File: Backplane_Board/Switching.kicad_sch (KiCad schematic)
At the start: 20 parts, among them J30 Conn_01x02, J31 Conn_01x02, Q3 ZXMN3A14F, Q4 ZXMN3A14F

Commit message: ready for final schmatic review
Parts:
- added C22, C23, C24, C25: 2.2uF+/35V+, Capacitor_SMD:C_0805_2012Metric, symbol Adafruit MOSFET Driver STEMMA Breakout-eagle-import:CAP_CERAMIC0805-NOOUTLINE
- added D16, D19, D22, D25: LED_Red, LED_SMD:LED_0603_1608Metric, symbol Device:LED
- added D17, D18, D23, D24: LED_Green, LED_SMD:LED_0603_1608Metric, symbol Device:LED
- added D20, D21, D26, D27: SM4002, Diode_SMD:D_SOD-123F, symbol Diode:SM4002
- added F3, F4, F5, F6: Fuse, Fuse:Fuse_0805_2012Metric, symbol Device:Fuse
- added J32, J33, J34, J35: Conn_01x02, Rpi_Pico_header:Molex_Micro-Latch_53253-0270_1x02_P2.00mm_Vertical_3D_model, symbol Connector_Generic:Conn_01x02
- added Q5, Q6, Q7, Q8: ZXMN3A14F, Package_TO_SOT_SMD:SOT-23, symbol Transistor_FET:ZXMN3A14F
- added R32, R33, R34, R35, R36, R37, R38, R39, R40, R41, R42, R43: 10k, Resistor_SMD:R_0805_2012Metric, symbol Adafruit MOSFET Driver STEMMA Breakout-eagle-import:RESISTOR_0603_NOOUT
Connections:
- net +12V: now also F4.2, F6.2
- net +5V: now also F3.2, F5.2
- net GND: now also C22.2, C23.2, C24.2, C25.2, D16.1 (K), D17.1 (K), D18.1 (K), D19.1 (K), D22.1 (K), D23.1 (K), D24.1 (K), D25.1 (K), Q5.2 (S), Q6.2 (S), Q7.2 (S), Q8.2 (S), R36.1, R37.1, R42.1, R43.1
- net SW1: now also Q6.1 (G), R33.2, R37.2; no longer Q3.1 (G), R26.2, R28.2
- net SW5: now also Q7.1 (G), R38.2, R42.2; no longer Q4.1 (G), R29.2, R31.2
- new net: C25.1, D26.1 (K), F5.1, J34.1 (Pin_1), R40.2
- new net: D24.2 (A), R40.1
- new net: D27.2 (A), J35.2 (Pin_2), Q8.3 (D)
- new net: D16.2 (A), R32.1
- new net: D19.2 (A), R33.1
- new net: D22.2 (A), R38.1
- new net: C22.1, D21.1 (K), F4.1, J33.1 (Pin_1), R35.2
- new net: D21.2 (A), J33.2 (Pin_2), Q6.3 (D)
- new net: D17.2 (A), R35.1
- new net: D26.2 (A), J34.2 (Pin_2), Q7.3 (D)
- new net: D23.2 (A), R41.1
- new net: D25.2 (A), R39.1
- new net: C24.1, D27.1 (K), F6.1, J35.1 (Pin_1), R41.2
- new net: C23.1, D20.1 (K), F3.1, J32.1 (Pin_1), R34.2
- new net: D20.2 (A), J32.2 (Pin_2), Q5.3 (D)
- new net: D18.2 (A), R34.1
- new net SW0: Q3.1 (G), R26.2, R28.2
- new net SW2: Q8.1 (G), R39.2, R43.2
- new net SW3: Q4.1 (G), R29.2, R31.2
- new net SW4: Q5.1 (G), R32.2, R36.2
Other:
- note added: "Note: I do not think this will work! We either need to look into a gate reiver IC, or must consider swaping to logic level fets"
- moved on the sheet: C20, C21, D10, D11, D12, D13, D14, D15, F1, F2, J30, J31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

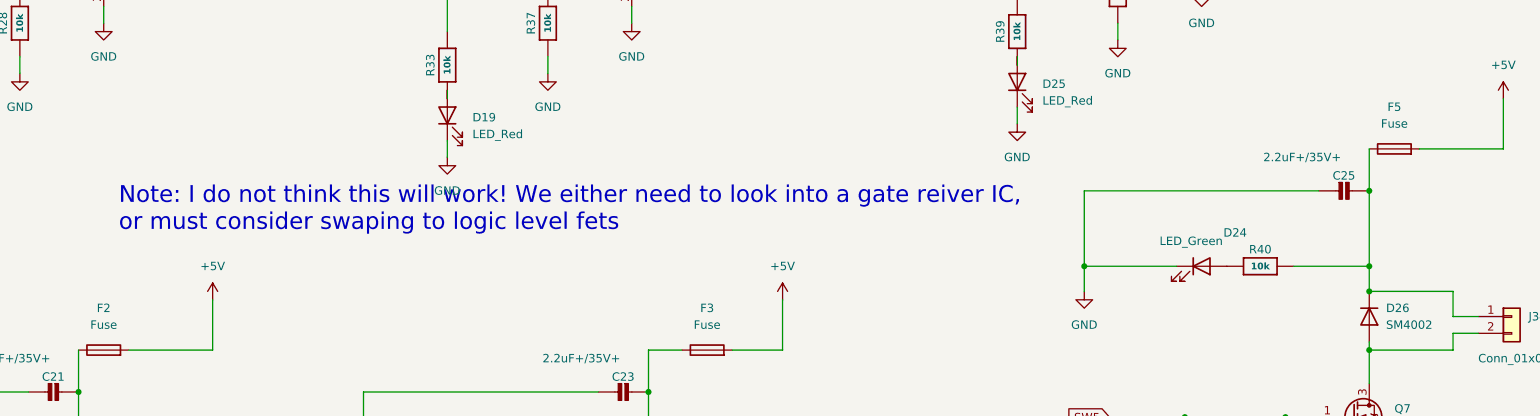
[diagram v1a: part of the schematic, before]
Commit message: updated i2c pullups to 3V3 logic, not isolator needed
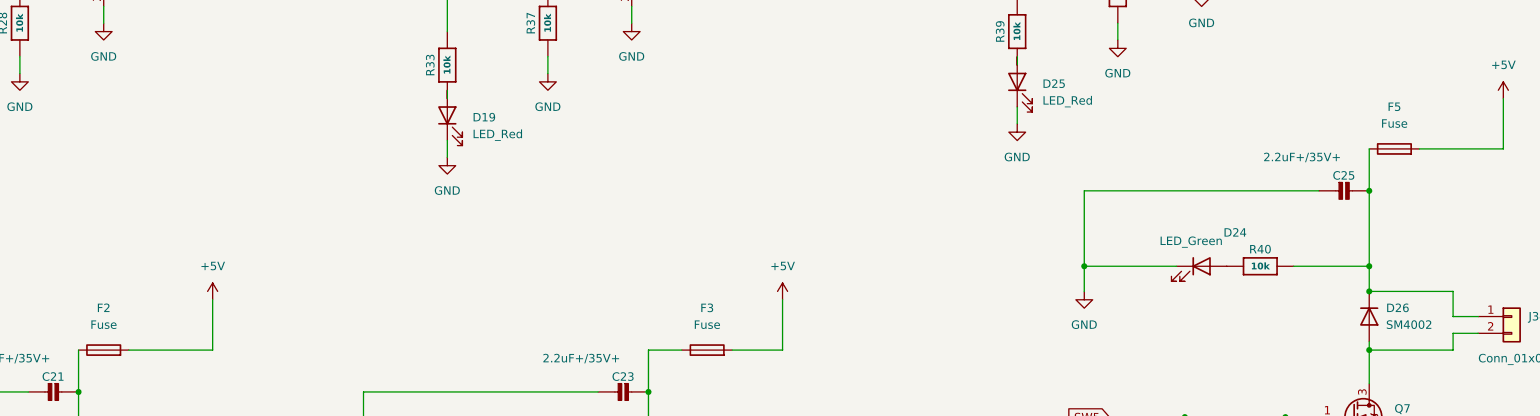
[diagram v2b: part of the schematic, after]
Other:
- note removed: "Note: I do not think this will work! We either need to look into a gate reiver IC, or must consider swaping to logic level fets"
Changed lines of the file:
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@@
-		)
-	)
-	(text "Note: I do not think this will work! We either need to look into a gate reiver IC,\nor must consider swaping to logic level fets"
-		(exclude_from_sim no)
-		(at 65.786 98.044 0)
-		(effects
-			(font
-				(size 2.54 2.54)
-				(color 255 81 93 1)
-			)
-			(justify left)
 		)
 	)

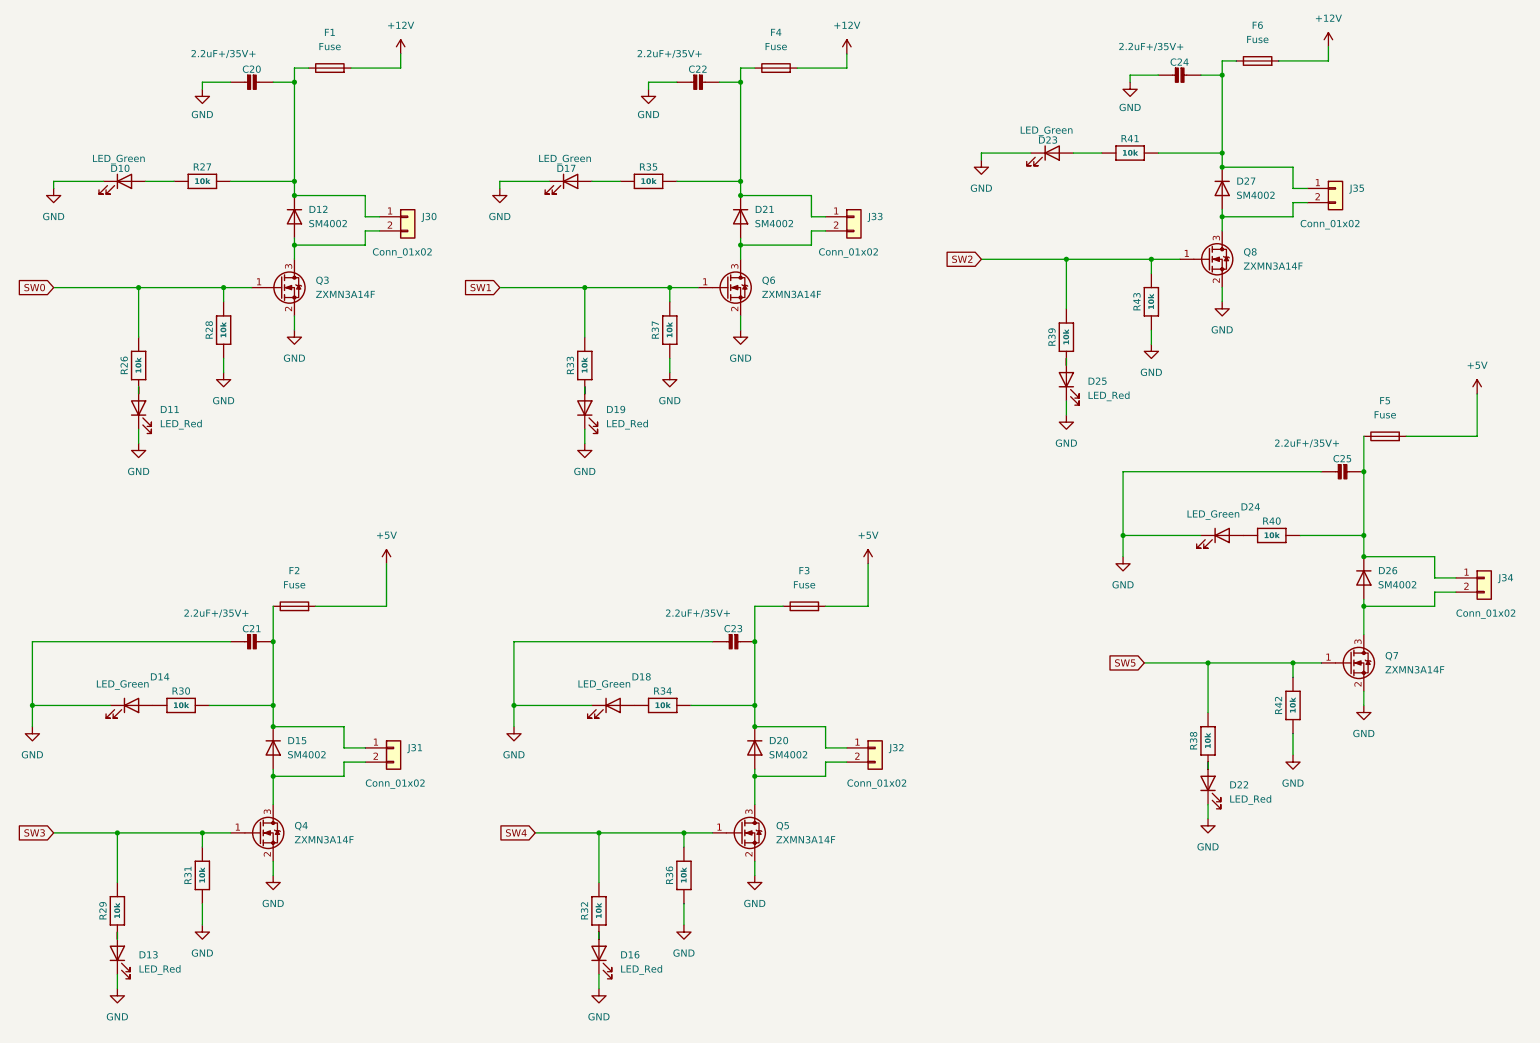
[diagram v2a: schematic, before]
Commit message: update FET circits
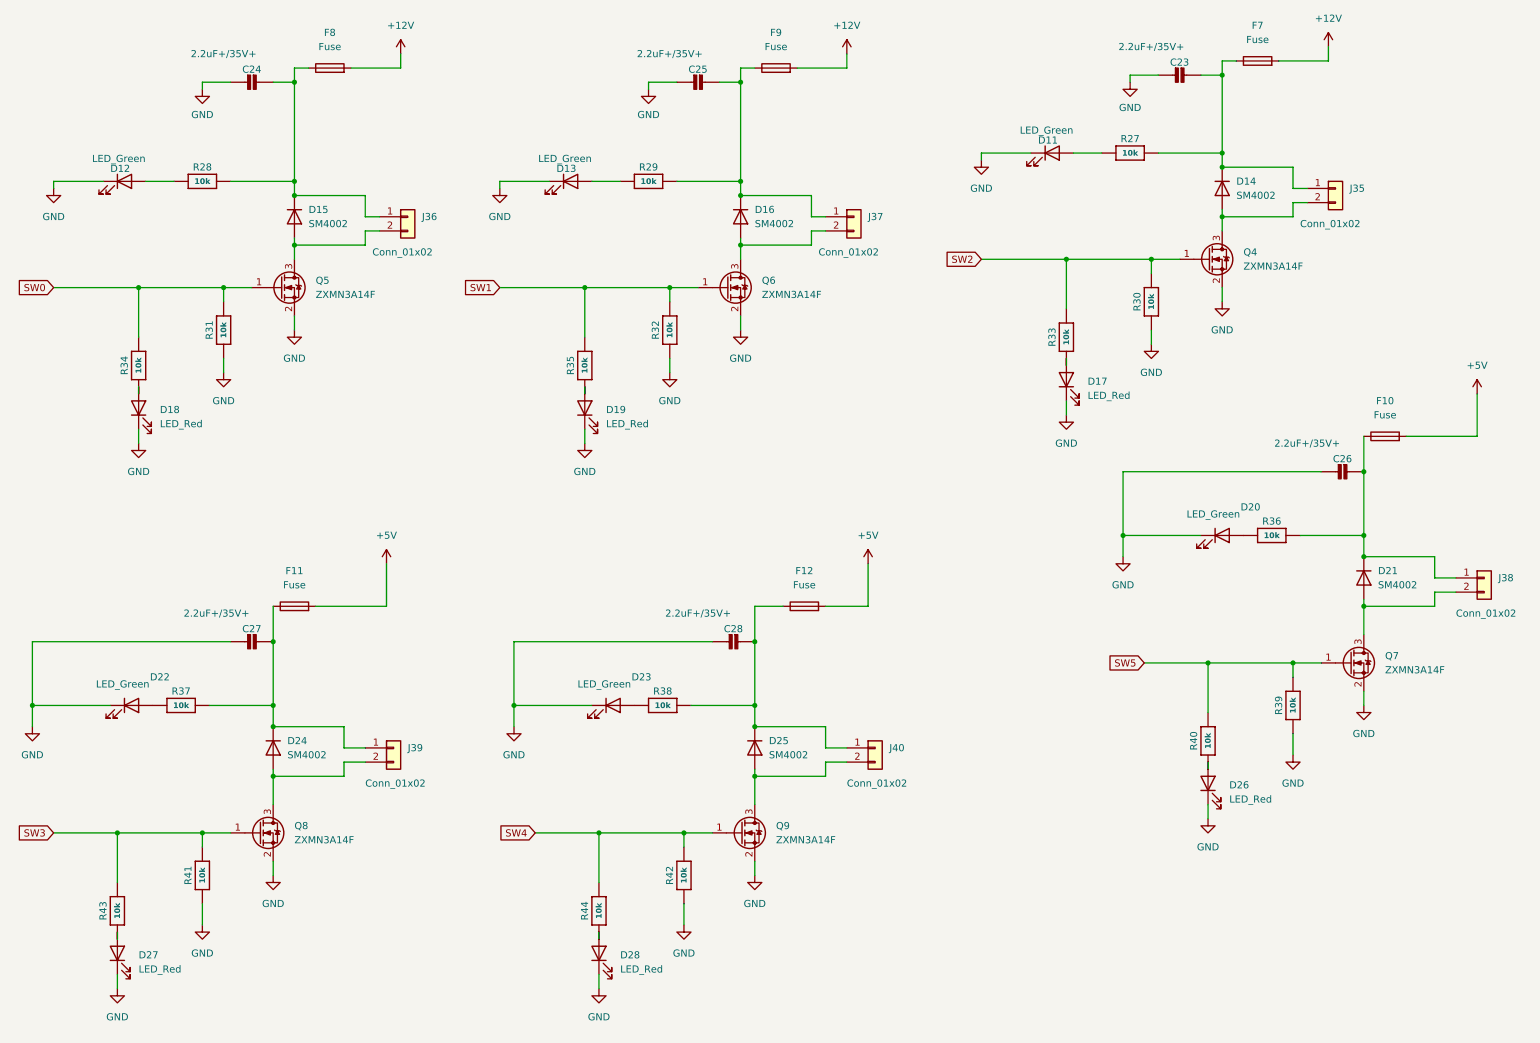
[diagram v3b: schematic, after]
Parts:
- renumbered C24 to C23, C20 to C24, C22 to C25, C25 to C26, C21 to C27, C23 to C28, D23 to D11, D10 to D12, D17 to D13, D27 to D14, D12 to D15, D21 to D16, D25 to D17, D11 to D18, D24 to D20, D26 to D21, D14 to D22, D18 to D23, D15 to D24, D20 to D25, D22 to D26, D13 to D27, D16 to D28, F5 to F10, F2 to F11, F3 to F12, F6 to F7, F1 to F8, F4 to F9, J30 to J36, J33 to J37, J34 to J38, J31 to J39, J32 to J40, Q8 to Q4, Q3 to Q5, Q4 to Q8, Q5 to Q9, R41 to R27, R27 to R28, R35 to R29, R43 to R30, R28 to R31, R37 to R32, R39 to R33, R26 to R34, R33 to R35, R40 to R36, R30 to R37, R34 to R38, R42 to R39, R38 to R40, R31 to R41, R36 to R42, R29 to R43, R32 to R44

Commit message: adding more footprints
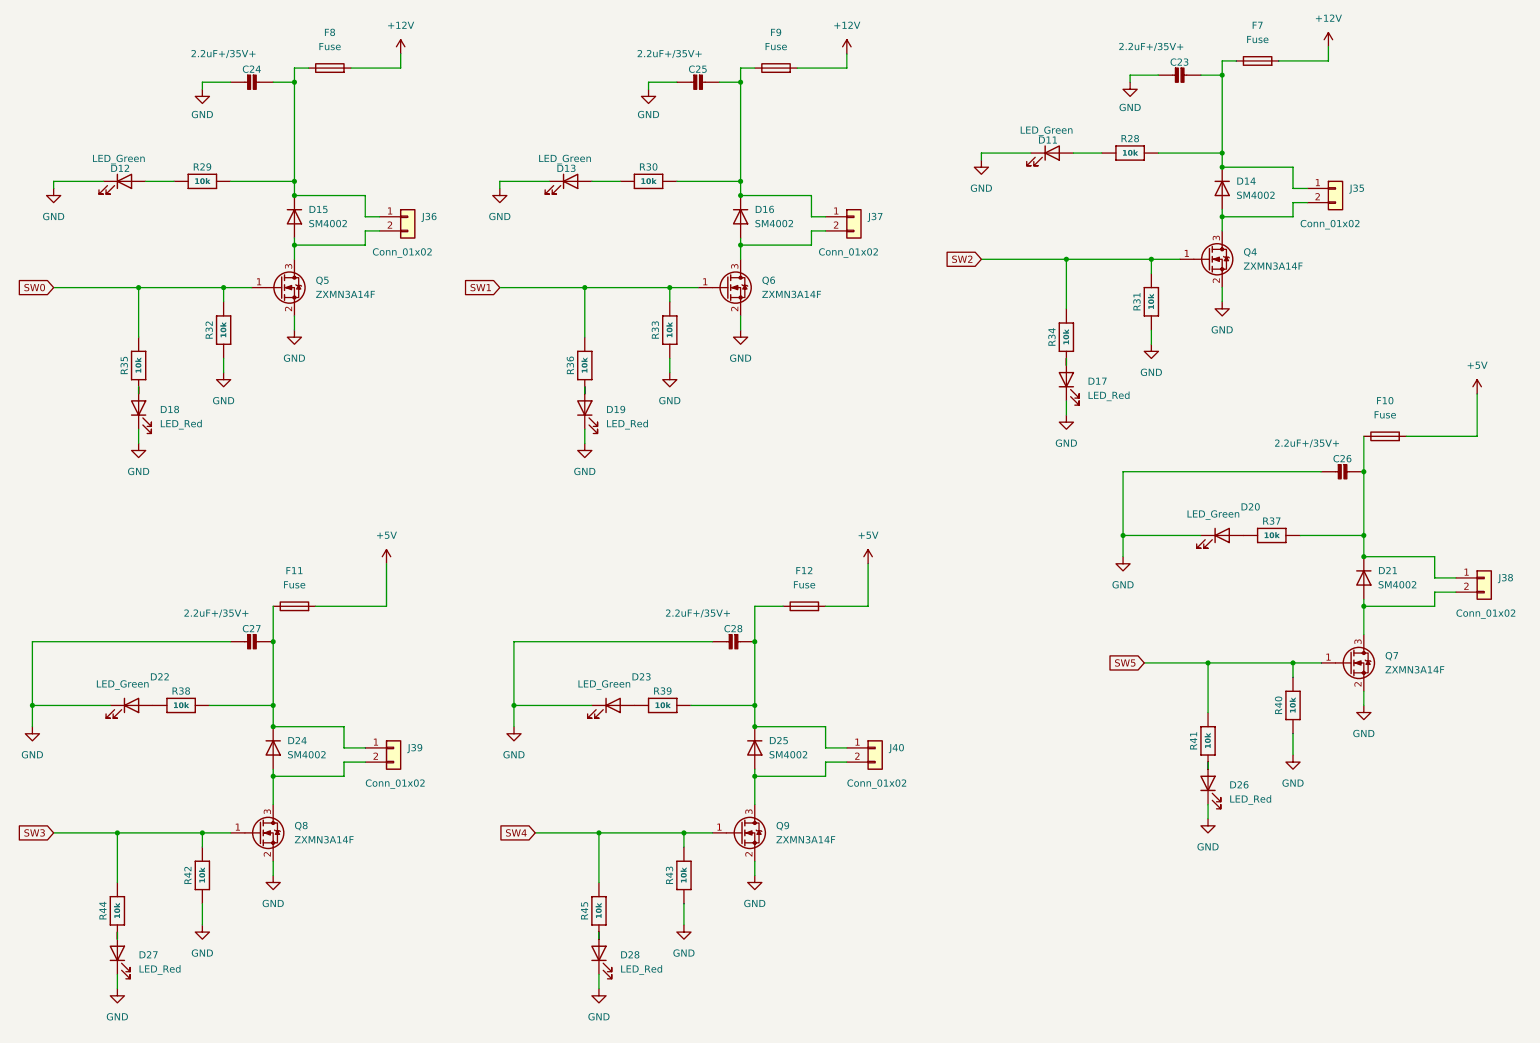
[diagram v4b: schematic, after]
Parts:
- renumbered R27 to R28, R28 to R29, R29 to R30, R30 to R31, R31 to R32, R32 to R33, R33 to R34, R34 to R35, R35 to R36, R36 to R37, R37 to R38, R38 to R39, R39 to R40, R40 to R41, R41 to R42, R42 to R43, R43 to R44, R44 to R45

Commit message: derat nest ifcation
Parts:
- J37: renamed from J35; footprint Rpi_Pico_header:Molex_Micro-Latch_53253-0270_1x02_P2.00mm_Vertical_3D_model -> Connector_Molex:Molex_Micro-Latch_53253-0270_1x02_P2.00mm_Vertical
- J38: renamed from J36; footprint Rpi_Pico_header:Molex_Micro-Latch_53253-0270_1x02_P2.00mm_Vertical_3D_model -> Connector_Molex:Molex_Micro-Latch_53253-0270_1x02_P2.00mm_Vertical
- J39: renamed from J37; footprint Rpi_Pico_header:Molex_Micro-Latch_53253-0270_1x02_P2.00mm_Vertical_3D_model -> Connector_Molex:Molex_Micro-Latch_53253-0270_1x02_P2.00mm_Vertical
- J40: renamed from J38; footprint Rpi_Pico_header:Molex_Micro-Latch_53253-0270_1x02_P2.00mm_Vertical_3D_model -> Connector_Molex:Molex_Micro-Latch_53253-0270_1x02_P2.00mm_Vertical
- J41: renamed from J39; footprint Rpi_Pico_header:Molex_Micro-Latch_53253-0270_1x02_P2.00mm_Vertical_3D_model -> Connector_Molex:Molex_Micro-Latch_53253-0270_1x02_P2.00mm_Vertical
- J42: renamed from J40; footprint Rpi_Pico_header:Molex_Micro-Latch_53253-0270_1x02_P2.00mm_Vertical_3D_model -> Connector_Molex:Molex_Micro-Latch_53253-0270_1x02_P2.00mm_Vertical
- renumbered C23 to C21, C24 to C22, C25 to C23, C26 to C24, C27 to C25, C28 to C26
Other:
- moved on the sheet: C24, F12
